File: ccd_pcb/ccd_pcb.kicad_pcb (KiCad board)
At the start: 2 copper layers, 91 x 88 mm, 50 parts, among them J1 Extension North, J2 Extension South, J3 PMODx2 North, J5 PMOD-Host-x1-GPIO, U1 ar0330CM, U2 ADP150-2.8, U3 TXS0108E, U4 TXS0108E, U5 TXS0108E

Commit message: redo layout
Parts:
- C12: moved to B.Cu
- C17: moved to F.Cu
- R1, R2, R8, R9: footprint Resistors_SMD:R_0805_HandSoldering -> Resistors_SMD:R_0603_HandSoldering
- R3, R4, R5, R6, R7: footprint Resistors_SMD:R_0805_HandSoldering -> Resistors_SMD:R_0603_HandSoldering; moved to F.Cu
- moved C1 99.7 mm to (-13.2, 4.75)
- moved C10 99.7 mm to (-12.5, 13.0)
- moved C13 99.7 mm to (-12.2, 9.00)
- moved C18 99.7 mm to (-18.8, 5.75)
- moved C24 99.7 mm to (-19.0, 14.0)
- moved C25 99.7 mm to (-18.8, 10.2)
- moved J3 79.0 mm to (56.9, 4.50)
- moved J1 72.4 mm to (33.5, 79.1)
- moved J2 72.4 mm to (62.0, 79.1)
- moved C22 71.5 mm to (38.0, 84.0)
- moved C27 71.5 mm to (66.9, 84.0)
- moved C8 70.6 mm to (-13.6, 24.1)
- moved R1 70.6 mm to (-13.5, 26.1)
- moved R2 70.6 mm to (-13.5, 28.0)
- moved C21 70.0 mm to (62.0, 84.0), turned to 0 degrees
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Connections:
- A1 pad 10: IO7_S -> LVDSs2_P
- A1 pad 100: /SLVS2_N -> PMOD4_S
- A1 pad 104: /SLVS3_P -> PMOD3_S
- A1 pad 106: /SLVS3_N -> PMOD2_S
- A1 pad 108: /SLVC_P -> PMOD1_S
- A1 pad 11: IO6_N -> LVDSn5_N
- A1 pad 110: /SLVC_N -> PMOD0_S
- A1 pad 12: IO6_S -> LVDSs2_N
- A1 pad 13: IO5_N -> LVDSn4_P
- A1 pad 14: IO5_S -> LVDSs1_P
- A1 pad 15: IO4_N -> LVDSn4_N
- A1 pad 16: IO4_S -> LVDSs1_N
- A1 pad 21: IO3_N -> LVDSn3_P
- A1 pad 22: IO3_S -> LVDSs0_P
- A1 pad 23: IO2_N -> LVDSn3_N
- A1 pad 24: IO2_S -> LVDSs0_N
- A1 pad 25: IO1_N -> LVDSn2_P
- A1 pad 26: IO1_S -> LVDSs4_P
- A1 pad 27: IO0_N -> LVDSn2_N
- A1 pad 28: IO0_S -> LVDSs4_N
- A1 pad 31: LVDSn0_P -> LVDSn1_P
- A1 pad 32: LVDSs0_P -> LVDSs5_P
- A1 pad 33: LVDSn0_N -> LVDSn1_N
- A1 pad 34: LVDSs0_N -> LVDSs5_N
- A1 pad 35: LVDSn1_P -> LVDSn0_P
- A1 pad 36: LVDSs1_P -> LVDSs3_P
- A1 pad 37: LVDSn1_N -> LVDSn0_N
- A1 pad 38: LVDSs1_N -> LVDSs3_N
- A1 pad 41: LVDSn2_P -> IO7_N
- A1 pad 42: LVDSs2_P -> IO7_S
- A1 pad 43: LVDSn2_N -> IO6_N
- A1 pad 44: LVDSs2_N -> IO6_S
- A1 pad 45: LVDSn5_P -> IO5_N
- A1 pad 46: LVDSs4_P -> IO5_S
- A1 pad 47: LVDSn5_N -> IO4_N
- A1 pad 48: LVDSs4_N -> IO4_S
- A1 pad 51: LVDSn3_P -> IO3_N
- A1 pad 52: LVDSs5_P -> IO3_S
- A1 pad 53: LVDSn3_N -> IO2_N
- A1 pad 54: LVDSs5_N -> IO2_S
- A1 pad 55: LVDSn4_P -> IO1_N
- A1 pad 56: LVDSs3_P -> IO1_S
- A1 pad 57: LVDSn4_N -> IO0_N
- A1 pad 58: LVDSs3_N -> IO0_S
- A1 pad 61: PMOD3_E -> FLASH
- A1 pad 62: PMOD7_S -> PMOD3_E
- A1 pad 63: PMOD2_E -> SHUTTER
- A1 pad 64: PMOD6_S -> PMOD2_E
- A1 pad 65: PMOD1_E -> SLVS0_P
- A1 pad 66: PMOD5_S -> PMOD1_E
- A1 pad 67: PMOD0_E -> SLVS0_N
- A1 pad 68: PMOD4_S -> PMOD0_E
- A1 pad 71: PMOD7_N -> SLVS1_P
- A1 pad 73: PMOD6_N -> SLVS1_N
- A1 pad 74: PMOD3_S -> PMOD7_N
- A1 pad 75: PMOD5_N -> SLVSC_P
- A1 pad 76: PMOD2_S -> PMOD6_N
- A1 pad 77: PMOD4_N -> SLVSC_N
- A1 pad 78: PMOD1_S -> PMOD5_N
- A1 pad 80: PMOD0_S -> PMOD4_N
- A1 pad 83: PMOD3_N -> SLVS2_P
- A1 pad 84: Net-(A1-Pad84) -> PMOD3_N
- A1 pad 85: PMOD2_N -> SLVS2_N
- A1 pad 86: Net-(A1-Pad86) -> PMOD2_N
- A1 pad 87: PMOD1_N -> SLVS3_P
- A1 pad 88: /SLVS0_P -> PMOD1_N
- A1 pad 89: PMOD0_N -> SLVS3_N
- A1 pad 9: IO7_N -> LVDSn5_P
- A1 pad 90: /SLVS0_N -> PMOD0_N
- A1 pad 94: /SLVS1_P -> PMOD7_S
- A1 pad 96: /SLVS1_N -> PMOD6_S
- A1 pad 98: /SLVS2_P -> PMOD5_S
- R3 pad 1: /SLVC_P -> SLVS0_P
- R3 pad 2: /SLVC_N -> SLVS0_N
- R4 pad 1: /SLVS3_P -> SLVS1_P
- R4 pad 2: /SLVS3_N -> SLVS1_N
- R5 pad 1: /SLVS2_P -> SLVS2_P
- R5 pad 2: /SLVS2_N -> SLVS2_N
- R6 pad 1: /SLVS1_P -> SLVS3_P
- R6 pad 2: /SLVS1_N -> SLVS3_N
- R7 pad 1: /SLVS0_P -> SLVSC_P
- R7 pad 2: /SLVS0_N -> SLVSC_N
- U1 pad 19: /SLVS0_N -> SLVS0_N
- U1 pad 20: /SLVS0_P -> SLVS0_P
- U1 pad 21: /SLVS1_P -> SLVS1_N
- U1 pad 22: /SLVS1_N -> SLVS1_P
- U1 pad 25: /SLVC_N -> SLVSC_N
- U1 pad 26: /SLVC_P -> SLVSC_P
- U1 pad 27: /SLVS2_N -> SLVS2_N
- U1 pad 28: /SLVS2_P -> SLVS2_P
- U1 pad 29: /SLVS3_N -> SLVS3_N
- U1 pad 3: Net-(A1-Pad86) -> FLASH
- U1 pad 30: /SLVS3_P -> SLVS3_P
- U1 pad 35: Net-(A1-Pad84) -> SHUTTER
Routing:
- net GNDA: track 0.00 -> 160.6 mm, vias 0 -> 2
- net /SLVS3_N: track 107.9 -> 0.00 mm, vias 1 -> 0
- net /SLVS2_N: track 104.0 -> 0.00 mm, vias 1 -> 0
- net /SLVS2_P: track 103.6 -> 0.00 mm, vias 1 -> 0
- net /SLVS3_P: track 103.3 -> 0.00 mm, vias 1 -> 0
- net /SLVS0_N: track 102.8 -> 0.00 mm, vias 1 -> 0
- net /SLVC_N: track 102.2 -> 0.00 mm, vias 1 -> 0
- net /SLVC_P: track 100.8 -> 0.00 mm, vias 1 -> 0
- net /SLVS0_P: track 100.2 -> 0.00 mm, vias 1 -> 0
- net PMOD7_S: track 68.2 -> 0.00 mm, vias 2 -> 0
- net PMOD6_S: track 68.2 -> 0.00 mm, vias 2 -> 0
- net LVDSs4_P: track 100.0 -> 39.1 mm
- net LVDSs4_N: track 100.1 -> 40.0 mm
- net LVDSs1_P: track 108.7 -> 49.0 mm
- net LVDSs2_P: track 100.2 -> 43.2 mm
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- added copper zone on B.Cu, net GNDA
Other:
- board size 91 x 88 mm -> 91 x 85 mm

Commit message: most of the routing done
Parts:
- C1, C10, C13, C17, C18: moved to B.Cu
- C4, C8: moved to F.Cu
- moved C18 83.0 mm to (54.9, 44.0)
- moved C13 71.0 mm to (44.3, 51.9), turned to 270 degrees
- moved R2 60.6 mm to (47.1, 29.6), turned to 90 degrees
- moved C17 59.2 mm to (48.3, 51.9), turned to 270 degrees
- moved C1 58.9 mm to (36.1, 37.0), turned to 180 degrees
- moved R1 58.8 mm to (45.1, 30.7), turned to 90 degrees
- moved C10 50.6 mm to (30.0, 40.4), turned to 90 degrees
- moved C25 47.9 mm to (-31.1, 56.5)
- moved C19 44.3 mm to (35.1, 40.8)
- moved C24 40.2 mm to (-31.0, 52.4)
- moved C26 35.4 mm to (23.2, 39.4), turned to 0 degrees
- moved C8 24.2 mm to (-29.9, 6.28)
- moved C4 24.1 mm to (-30.0, 11.2), turned to 0 degrees
- moved C3 18.7 mm to (25.8, 29.6)
- moved U2 18.7 mm to (29.1, 29.6)
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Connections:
- A1 pad 100: PMOD4_S -> PMOD3_S
- A1 pad 103: LED1 -> LED2
- A1 pad 104: PMOD3_S -> PMOD4_S
- A1 pad 106: PMOD2_S -> PMOD5_S
- A1 pad 108: PMOD1_S -> PMOD6_S
- A1 pad 110: PMOD0_S -> PMOD7_S
- A1 pad 41: IO7_N -> IO6_N
- A1 pad 42: IO7_S -> IO6_S
- A1 pad 43: IO6_N -> IO7_N
- A1 pad 44: IO6_S -> IO7_S
- A1 pad 45: IO5_N -> IO4_N
- A1 pad 46: IO5_S -> IO4_S
- A1 pad 47: IO4_N -> IO5_N
- A1 pad 48: IO4_S -> IO5_S
- A1 pad 51: IO3_N -> IO2_N
- A1 pad 53: IO2_N -> IO3_N
- A1 pad 55: IO1_N -> IO0_N
- A1 pad 57: IO0_N -> IO1_N
- A1 pad 62: PMOD3_E -> PMOD0_E
- A1 pad 64: PMOD2_E -> PMOD1_E
- A1 pad 66: PMOD1_E -> PMOD2_E
- A1 pad 68: PMOD0_E -> PMOD3_E
- A1 pad 74: PMOD7_N -> PMOD0_N
- A1 pad 76: PMOD6_N -> PMOD1_N
- A1 pad 78: PMOD5_N -> PMOD2_N
- A1 pad 80: PMOD4_N -> PMOD7_N
- A1 pad 84: PMOD3_N -> PMOD6_N
- A1 pad 86: PMOD2_N -> PMOD5_N
- A1 pad 88: PMOD1_N -> PMOD4_N
- A1 pad 90: PMOD0_N -> PMOD3_N
- A1 pad 93: LED2 -> LED1
- A1 pad 94: PMOD7_S -> PMOD0_S
- A1 pad 96: PMOD6_S -> PMOD1_S
- A1 pad 98: PMOD5_S -> PMOD2_S
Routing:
- net GNDA: track 160.6 -> 524.9 mm, vias 2 -> 14
- net /3V3: track 61.7 -> 280.4 mm, vias 0 -> 6
- net /1V8: track 15.5 -> 219.4 mm, vias 0 -> 3
- net /5V: track 34.3 -> 178.7 mm, vias 0 -> 6
- net IO0_N: track 0.00 -> 85.8 mm, vias 0 -> 1
- net IO2_N: track 0.00 -> 85.4 mm, vias 0 -> 1
- net IO1_N: track 0.00 -> 80.8 mm, vias 0 -> 1
- net IO3_N: track 0.00 -> 80.7 mm, vias 0 -> 1
- net SDA_N: track 0.00 -> 79.7 mm, vias 0 -> 2
- net PMOD3_E: track 0.00 -> 75.1 mm, vias 0 -> 2
- net PMOD1_E: track 0.00 -> 75.1 mm, vias 0 -> 2
- net PMOD2_E: track 0.00 -> 75.0 mm, vias 0 -> 2
- net SCL_N: track 0.00 -> 74.3 mm, vias 0 -> 2
- net PMOD0_E: track 0.00 -> 73.8 mm, vias 0 -> 2
- net IO5_N: track 0.00 -> 73.3 mm, vias 0 -> 1
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
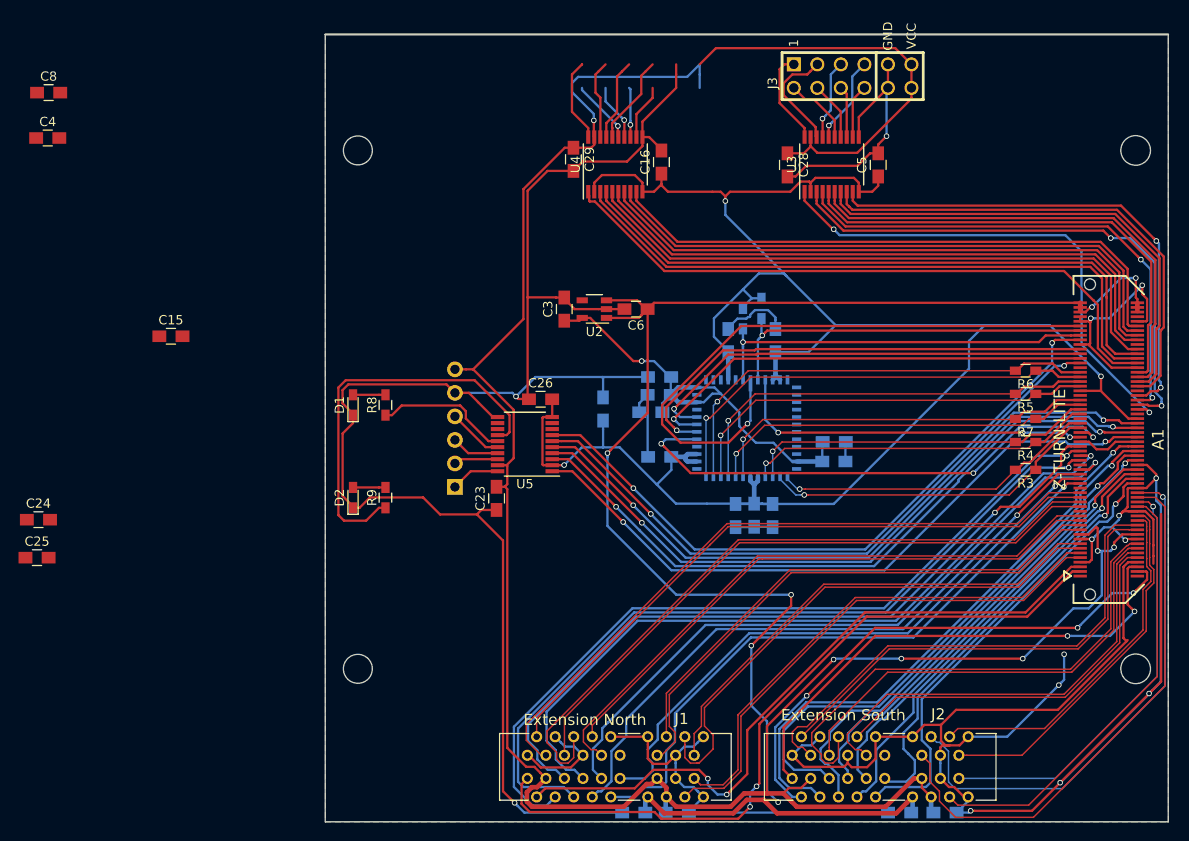
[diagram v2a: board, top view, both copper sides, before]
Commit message: done routing; length matching and via stitching not done yet
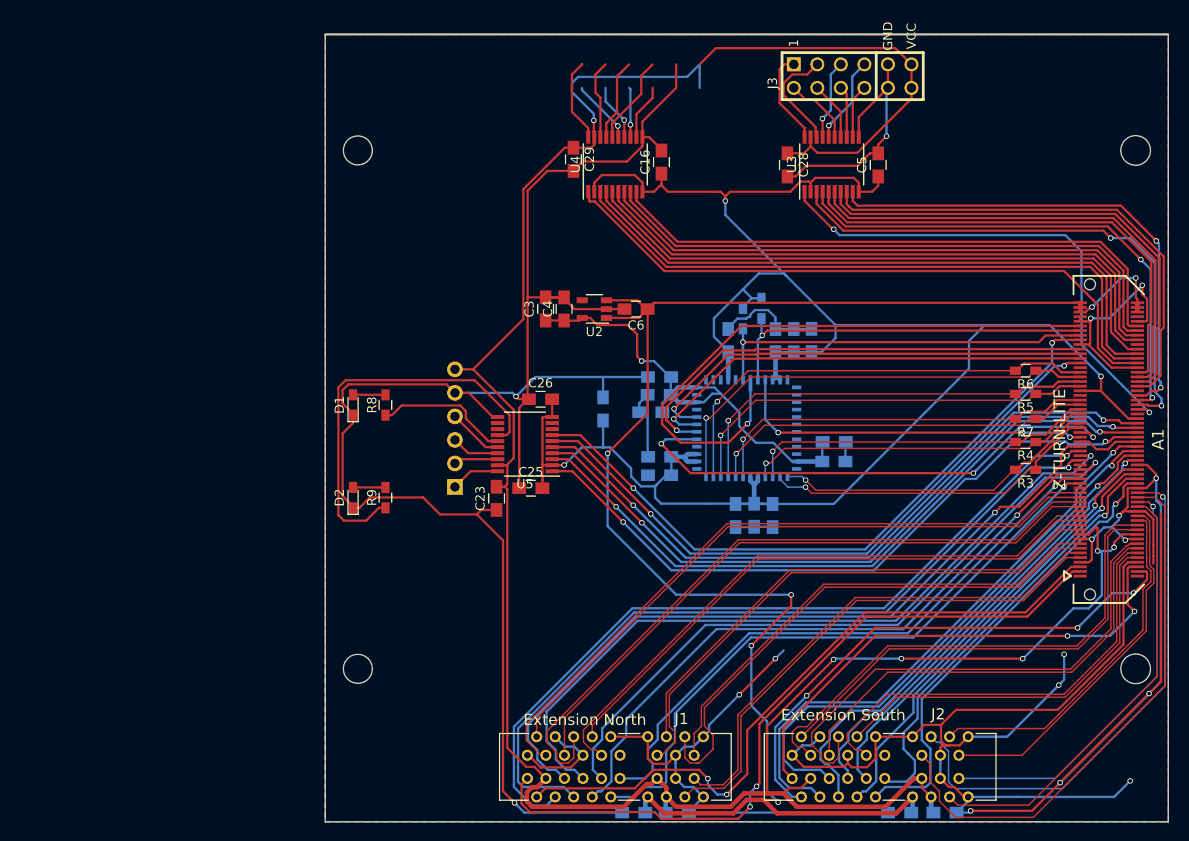
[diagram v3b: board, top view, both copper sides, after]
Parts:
- C15, C24, C8: moved to B.Cu
- moved C24 85.7 mm to (52.5, 33.0), turned to 270 degrees
- moved C8 84.8 mm to (50.6, 33.0), turned to 90 degrees
- moved C4 58.7 mm to (25.8, 29.6), turned to 90 degrees
- moved C15 54.8 mm to (36.1, 47.6), turned to 180 degrees
- moved C25 53.8 mm to (22.2, 49.0)
- moved C3 2.01 mm to (23.8, 29.6)
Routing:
- net GNDA: track 524.9 -> 571.7 mm, vias 14 -> 17
- net /1V8: track 219.4 -> 228.5 mm
- net /2V8: track 47.6 -> 51.0 mm
- added copper zone on F.Cu, net GNDA

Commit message: almost finished
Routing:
- net GNDA: track 571.7 -> 902.4 mm, vias 17 -> 52
- net LVDSs4_N: track 39.7 -> 75.7 mm
- net LVDSs4_P: track 38.9 -> 74.9 mm
- net LVDSs2_P: track 43.2 -> 71.1 mm
- net LVDSs2_N: track 47.8 -> 75.7 mm
- net LVDSs1_P: track 48.3 -> 75.7 mm
- net LVDSs0_P: track 50.8 -> 76.1 mm
- net LVDSs0_N: track 55.4 -> 75.3 mm
- net LVDSs1_N: track 55.6 -> 75.5 mm
- net LVDSn5_N: track 55.8 -> 75.0 mm
- net LVDSn5_P: track 56.9 -> 75.9 mm
- net LVDSn3_P: track 59.6 -> 75.7 mm
- net LVDSn3_N: track 56.9 -> 72.9 mm
- net SLVS0_N: track 35.2 -> 49.6 mm
- net SLVS0_P: track 36.7 -> 51.2 mm
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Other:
- board text added: "AXIOM µ"
- board text added: "v 1.0"

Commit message: closes #21;
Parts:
- removed C8: .1µF, Capacitors_SMD:C_0805_HandSoldering
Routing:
- net IO7_N: track 66.1 -> 66.6 mm

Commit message: minor improvments
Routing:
- net LVDSn4_P: track 58.8 -> 79.6 mm
- net LVDSn4_N: track 54.4 -> 75.1 mm
- net GNDA: track 902.4 -> 909.9 mm
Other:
- net class Default: clearance 0.2 -> 0.152
- net class lvds: clearance 0.16 -> 0.152
- net class power: clearance 0.2 -> 0.152
- rule trace_clearance: 0.2 -> 0.152

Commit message: some minor bugfixes
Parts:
- added ?: mounting_hole, mounting_hole:mounting_hole, F.Cu at (87.3, 68.9)
- added ?: mounting_hole, mounting_hole:mounting_hole, F.Cu at (3.09, 12.7)
- added ?: mounting_hole, mounting_hole:mounting_hole, F.Cu at (3.52, 68.5)
- added ?: mounting_hole, mounting_hole:mounting_hole, F.Cu at (87.9, 12.6)
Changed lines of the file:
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@@
     (links 279)
     (no_connects 0)
-    (area -0.050001 -0.050001 91.050001 85.050001)
+    (area -13.849999 -5.7 91.3852 85.107)
     (thickness 1.6)
     (drawings 17)
     (tracks 7278)
     (zones 0)
-    (modules 50)
+    (modules 54)
     (nets 114)
   )
@@
     (mod_text_size 1 1)
     (mod_text_width 0.15)
-    (pad_size 1.7 1.7)
-    (pad_drill 1)
+    (pad_size 3.124 3.124)
+    (pad_drill 3.124)
     (pad_to_mask_clearance 0)
     (aux_axis_origin 35 39)
@@
     (visible_elements FFFFEF7F)
     (pcbplotparams
-      (layerselection 0x00030_80000001)
+      (layerselection 0x010f0_80000001)
       (usegerberextensions false)
       (excludeedgelayer true)
@@
       (outputformat 1)
       (mirror false)
-      (drillshape 1)
+      (drillshape 0)
       (scaleselection 1)
-      (outputdirectory ""))
+      (outputdirectory gerber/))
   )
   (net 0 "")
@@
     (uvia_drill 0.1)
   )
+  (module mounting_hole:mounting_hole (layer F.Cu)
+    (at 87.29 68.88)
+    (fp_text reference "" (at 0 -5.08) (layer F.SilkS)
+      (effects (font (size 1 1) (thickness 0.15)))
+    )
+    (fp_text value mounting_hole (at -2.3 -3.5) (layer F.Fab)
+      (effects (font (size 1 1) (thickness 0.15)))
+    )
+    (pad "" np_thru_hole circle (at 0.19 -0.4) (size 3.124 3.124) (drill 3.124) (layers *.Cu *.Mask))
+  )
+  (module mounting_hole:mounting_hole (layer F.Cu)
+    (at 3.09 12.68)
+    (fp_text reference "" (at 0 -5.08) (layer F.SilkS)
+      (effects (font (size 1 1) (thickness 0.15)))
+    )
+    (fp_text value mounting_hole (at 3.3 -3.6) (layer F.Fab)
+      (effects (font (size 1 1) (thickness 0.15)))
+    )
+    (pad "" np_thru_hole circle (at 0.43 -0.16) (size 3.124 3.124) (drill 3.124) (layers *.Cu *.Mask))
+  )
   (module Resistors_SMD:R_0603_HandSoldering (layer F.Cu)
     (at 75.6 44 180)
@@
       (effects (font (size 1.2065 1.2065) (thickness 0.1016)) (justify left))
     )
-    (fp_text value "Extension South" (at -15.24 6.35) (layer F.SilkS)
+    (fp_text value "Extension South" (at -8.86 -5.78) (layer F.SilkS)
       (effects (font (size 1.2065 1.2065) (thickness 0.1016)) (justify left))
     )
@@
       (effects (font (size 1.2065 1.2065) (thickness 0.1016)) (justify left))
     )
-    (fp_text value "Extension North" (at -15.24 6.35) (layer F.SilkS)
+    (fp_text value "Extension North" (at -8.98 -4.88) (layer F.SilkS)
       (effects (font (size 1.2065 1.2065) (thickness 0.1016)) (justify left))
     )
@@
     (pad "" np_thru_hole circle (at 9.15 0) (size 2.15 2.15) (drill 2.15) (layers *.Cu *.Mask))
   )
-  (gr_text "v 1.0" (at 12.49 19.08 180) (layer F.Fab)
+  (module mounting_hole:mounting_hole (layer F.Cu)
+    (at 3.52 68.48)
+    (fp_text reference "" (at 0 -5.08) (layer F.SilkS)
+      (effects (font (size 1 1) (thickness 0.15)))
+    )
+    (fp_text value mounting_hole (at 3.37 -3.4) (layer F.Fab)
+      (effects (font (size 1 1) (thickness 0.15)))
+    )
+    (pad "" np_thru_hole circle (at 0 0) (size 3.124 3.124) (drill 3.124) (layers *.Cu *.Mask))
+  )
+  (module mounting_hole:mounting_hole (layer F.Cu)
+    (at 87.89 12.58)
+    (fp_text reference "" (at -0.4 -4.6) (layer F.SilkS)
+      (effects (font (size 1 1) (thickness 0.15)))
+    )
+    (fp_text value mounting_hole (at -2.8 -3) (layer F.Fab)
+      (effects (font (size 1 1) (thickness 0.15)))
+    )
+    (pad "" np_thru_hole circle (at -0.41 -0.06) (size 3.124 3.124) (drill 3.124) (layers *.Cu *.Mask))
+  )
+  (gr_text "v 1.0" (at 12.49 19.08 180) (layer F.SilkS)
     (effects (font (size 1.5 1.5) (thickness 0.3)))
   )
-  (gr_text "AXIOM µ" (at 10.79 21.78 180) (layer F.Fab)
+  (gr_text "AXIOM µ" (at 10.79 21.78 180) (layer F.SilkS)
     (effects (font (size 1.5 1.5) (thickness 0.3)))
   )
-  (gr_text "AXIOM µ" (at 10.69 21.68 180) (layer B.Fab)
+  (gr_text "AXIOM µ" (at 10.69 21.68 180) (layer B.SilkS)
     (effects (font (size 1.5 1.5) (thickness 0.3)) (justify mirror))
   )
